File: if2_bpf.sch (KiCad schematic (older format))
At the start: 16 parts

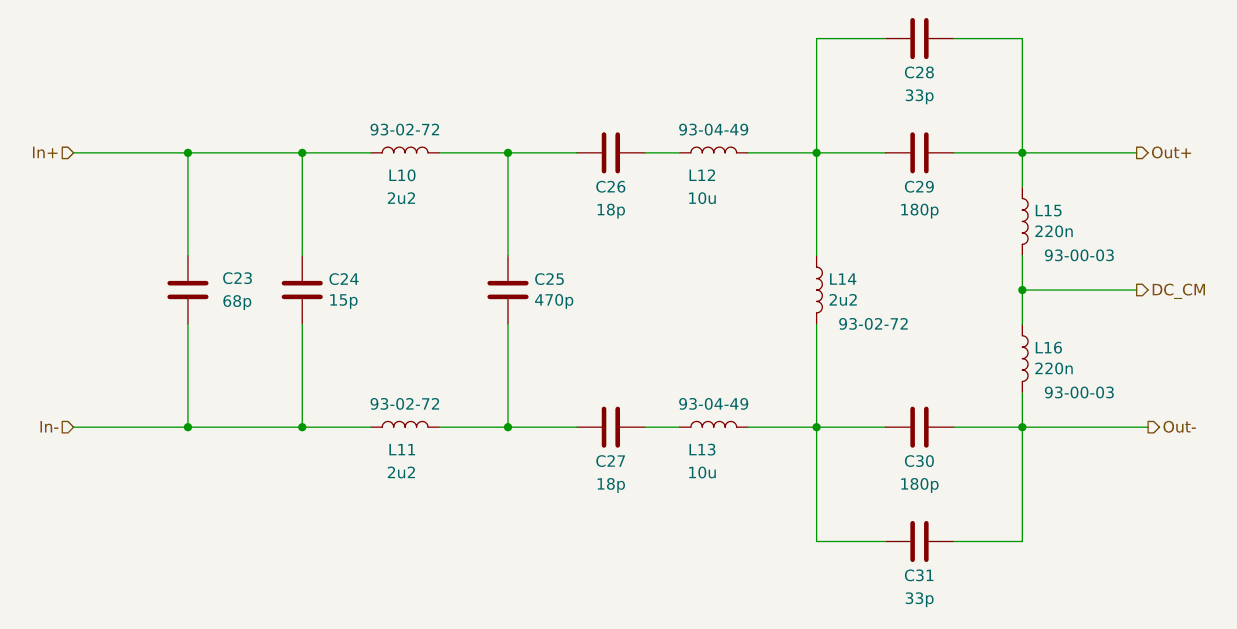
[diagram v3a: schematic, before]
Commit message: RX PCB revision: Diff amp + Mixer2
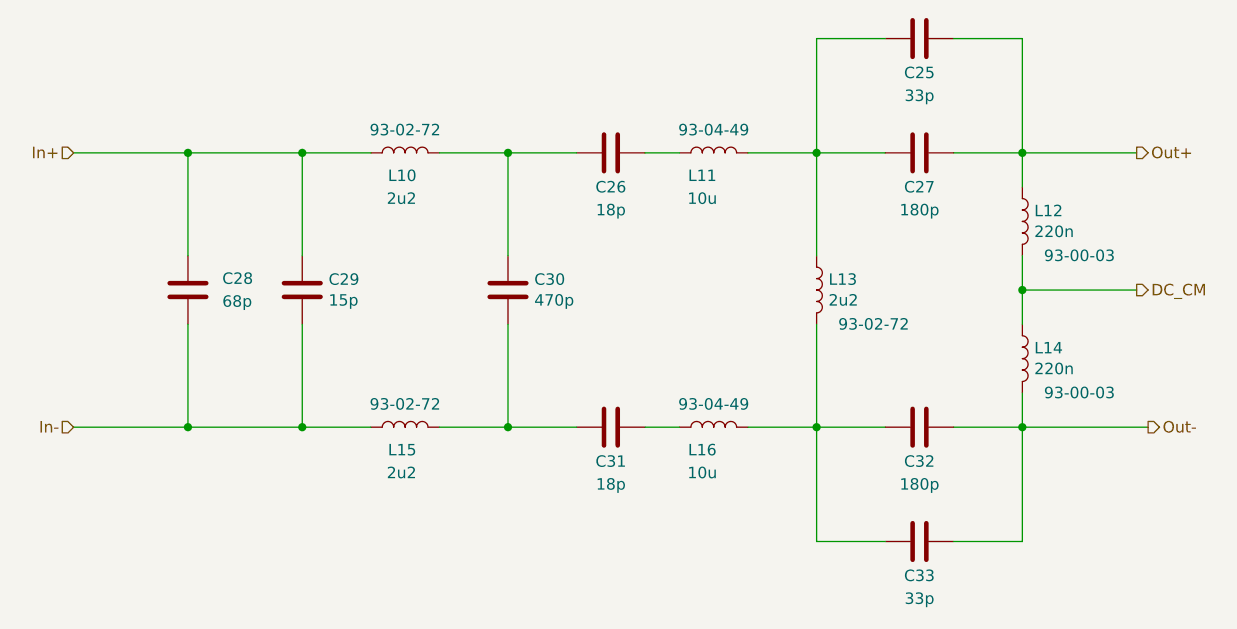
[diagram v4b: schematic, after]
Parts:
- C25: renamed from C28; footprint Capacitor_SMD:C_0805_2012Metric_Pad1.18x1.45mm_HandSolder -> Capacitor_SMD:C_0805_2012Metric_Pad1.15x1.40mm_HandSolder
- C26: footprint Capacitor_SMD:C_0805_2012Metric_Pad1.18x1.45mm_HandSolder -> Capacitor_SMD:C_0805_2012Metric_Pad1.15x1.40mm_HandSolder
- C27: renamed from C29; footprint Capacitor_SMD:C_0805_2012Metric_Pad1.18x1.45mm_HandSolder -> Capacitor_SMD:C_0805_2012Metric_Pad1.15x1.40mm_HandSolder
- C28: renamed from C23; footprint Capacitor_SMD:C_0805_2012Metric_Pad1.18x1.45mm_HandSolder -> Capacitor_SMD:C_0805_2012Metric_Pad1.15x1.40mm_HandSolder
- C29: renamed from C24; footprint Capacitor_SMD:C_0805_2012Metric_Pad1.18x1.45mm_HandSolder -> Capacitor_SMD:C_0805_2012Metric_Pad1.15x1.40mm_HandSolder
- C30: renamed from C25; footprint Capacitor_SMD:C_0805_2012Metric_Pad1.18x1.45mm_HandSolder -> Capacitor_SMD:C_0805_2012Metric_Pad1.15x1.40mm_HandSolder
- C31: renamed from C27; footprint Capacitor_SMD:C_0805_2012Metric_Pad1.18x1.45mm_HandSolder -> Capacitor_SMD:C_0805_2012Metric_Pad1.15x1.40mm_HandSolder
- C32: renamed from C30; footprint Capacitor_SMD:C_0805_2012Metric_Pad1.18x1.45mm_HandSolder -> Capacitor_SMD:C_0805_2012Metric_Pad1.15x1.40mm_HandSolder
- C33: renamed from C31; footprint Capacitor_SMD:C_0805_2012Metric_Pad1.18x1.45mm_HandSolder -> Capacitor_SMD:C_0805_2012Metric_Pad1.15x1.40mm_HandSolder
- renumbered L12 to L11, L15 to L12, L14 to L13, L16 to L14, L11 to L15, L13 to L16
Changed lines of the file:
@@
 $Descr A4 11693 8268
 encoding utf-8
-Sheet 6 7
+Sheet 5 7
 Title "9 MHz IF filter"
 Date "2021-01-15"
@@
 In-
 $Comp
-L Device:C C23
+L Device:C C28
 U 1 1 5FECCD6C
 P 4100 3950
-F 0 "C23" H 4250 4000 50  0000 L CNN
+F 0 "C28" H 4250 4000 50  0000 L CNN
 F 1 "68p" H 4250 3900 50  0000 L CNN
-F 2 "Capacitor_SMD:C_0805_2012Metric_Pad1.18x1.45mm_HandSolder" H 4138 3800 50  0001 C CNN
+F 2 "Capacitor_SMD:C_0805_2012Metric_Pad1.15x1.40mm_HandSolder" H 4138 3800 50  0001 C CNN
 F 3 "~" H 4100 3950 50  0001 C CNN
 	1    4100 3950
@@
 $EndComp
 $Comp
-L Device:C C24
+L Device:C C29
 U 1 1 5FECE707
 P 4600 3950
-F 0 "C24" H 4715 3996 50  0000 L CNN
+F 0 "C29" H 4715 3996 50  0000 L CNN
 F 1 "15p" H 4715 3905 50  0000 L CNN
-F 2 "Capacitor_SMD:C_0805_2012Metric_Pad1.18x1.45mm_HandSolder" H 4638 3800 50  0001 C CNN
+F 2 "Capacitor_SMD:C_0805_2012Metric_Pad1.15x1.40mm_HandSolder" H 4638 3800 50  0001 C CNN
 F 3 "~" H 4600 3950 50  0001 C CNN
 	1    4600 3950
@@
 F 0 "C26" V 6100 3350 50  0000 C CNN
 F 1 "18p" V 6200 3350 50  0000 C CNN
-F 2 "Capacitor_SMD:C_0805_2012Metric_Pad1.18x1.45mm_HandSolder" H 5988 3200 50  0001 C CNN
+F 2 "Capacitor_SMD:C_0805_2012Metric_Pad1.15x1.40mm_HandSolder" H 5988 3200 50  0001 C CNN
 F 3 "~" H 5950 3350 50  0001 C CNN
 	1    5950 3350
@@
 $EndComp
 $Comp
-L Device:L L12
+L Device:L L11
 U 1 1 5FECF5C4
 P 6400 3350
-F 0 "L12" V 6300 3400 50  0000 C CNN
+F 0 "L11" V 6300 3400 50  0000 C CNN
 F 1 "10u" V 6200 3400 50  0000 C CNN
 F 2 "Inductor_SMD:L_1210_3225Metric_Pad1.42x2.65mm_HandSolder" H 6400 3350 50  0001 C CNN
@@
 $EndComp
 $Comp
-L Device:L L14
+L Device:L L13
 U 1 1 5FED0166
 P 6850 3950
-F 0 "L14" H 6902 3996 50  0000 L CNN
+F 0 "L13" H 6902 3996 50  0000 L CNN
 F 1 "2u2" H 6902 3905 50  0000 L CNN
 F 2 "Inductor_SMD:L_0805_2012Metric_Pad1.15x1.40mm_HandSolder" H 6850 3950 50  0001 C CNN
@@
 $EndComp
 $Comp
-L Device:C C29
+L Device:C C27
 U 1 1 5FED1E6D
 P 7300 3350
-F 0 "C29" V 7450 3350 50  0000 C CNN
+F 0 "C27" V 7450 3350 50  0000 C CNN
 F 1 "180p" V 7550 3350 50  0000 C CNN
-F 2 "Capacitor_SMD:C_0805_2012Metric_Pad1.18x1.45mm_HandSolder" H 7338 3200 50  0001 C CNN
+F 2 "Capacitor_SMD:C_0805_2012Metric_Pad1.15x1.40mm_HandSolder" H 7338 3200 50  0001 C CNN
 F 3 "~" H 7300 3350 50  0001 C CNN
 	1    7300 3350
@@
 $EndComp
 $Comp
-L Device:L L15
+L Device:L L12
 U 1 1 5FED258A
 P 7750 3650
-F 0 "L15" H 7802 3696 50  0000 L CNN
+F 0 "L12" H 7802 3696 50  0000 L CNN
 F 1 "220n" H 7802 3605 50  0000 L CNN
 F 2 "Inductor_SMD:L_1210_3225Metric_Pad1.42x2.65mm_HandSolder" H 7750 3650 50  0001 C CNN
@@
 DC_CM
 $Comp
-L Device:C C30
+L Device:C C32
 U 1 1 5FED6CF7
 P 7300 4550
-F 0 "C30" V 7150 4550 50  0000 C CNN
+F 0 "C32" V 7150 4550 50  0000 C CNN
 F 1 "180p" V 7050 4550 50  0000 C CNN
-F 2 "Capacitor_SMD:C_0805_2012Metric_Pad1.18x1.45mm_HandSolder" H 7338 4400 50  0001 C CNN
+F 2 "Capacitor_SMD:C_0805_2012Metric_Pad1.15x1.40mm_HandSolder" H 7338 4400 50  0001 C CNN
 F 3 "~" H 7300 4550 50  0001 C CNN
 	1    7300 4550
@@
 $EndComp
 $Comp
-L Device:C C27
+L Device:C C31
 U 1 1 5FED7DBE
 P 5950 4550
-F 0 "C27" V 6100 4550 50  0000 C CNN
+F 0 "C31" V 6100 4550 50  0000 C CNN
 F 1 "18p" V 6200 4550 50  0000 C CNN
-F 2 "Capacitor_SMD:C_0805_2012Metric_Pad1.18x1.45mm_HandSolder" H 5988 4400 50  0001 C CNN
+F 2 "Capacitor_SMD:C_0805_2012Metric_Pad1.15x1.40mm_HandSolder" H 5988 4400 50  0001 C CNN
 F 3 "~" H 5950 4550 50  0001 C CNN
 	1    5950 4550
@@
 $EndComp
 $Comp
-L Device:C C25
+L Device:C C30
 U 1 1 5FEE51AD
 P 5500 3950
-F 0 "C25" H 5615 3996 50  0000 L CNN
+F 0 "C30" H 5615 3996 50  0000 L CNN
 F 1 "470p" H 5615 3905 50  0000 L CNN
-F 2 "Capacitor_SMD:C_0805_2012Metric_Pad1.18x1.45mm_HandSolder" H 5538 3800 50  0001 C CNN
+F 2 "Capacitor_SMD:C_0805_2012Metric_Pad1.15x1.40mm_HandSolder" H 5538 3800 50  0001 C CNN
 F 3 "~" H 5500 3950 50  0001 C CNN
 	1    5500 3950
@@
 $EndComp
 $Comp
-L Device:L L11
+L Device:L L15
 U 1 1 6002A199
 P 5050 4550
-F 0 "L11" V 4950 4500 50  0000 L CNN
+F 0 "L15" V 4950 4500 50  0000 L CNN
 F 1 "2u2" V 4850 4500 50  0000 L CNN
 F 2 "Inductor_SMD:L_0805_2012Metric_Pad1.15x1.40mm_HandSolder" H 5050 4550 50  0001 C CNN
@@
 $EndComp
 $Comp
-L Device:L L13
+L Device:L L16
 U 1 1 6002AC30
 P 6400 4550
-F 0 "L13" V 6300 4600 50  0000 C CNN
+F 0 "L16" V 6300 4600 50  0000 C CNN
 F 1 "10u" V 6200 4600 50  0000 C CNN
 F 2 "Inductor_SMD:L_1210_3225Metric_Pad1.42x2.65mm_HandSolder" H 6400 4550 50  0001 C CNN
@@
 $EndComp
 $Comp
-L Device:L L16
+L Device:L L14
 U 1 1 6002B609
 P 7750 4250
-F 0 "L16" H 7802 4296 50  0000 L CNN
+F 0 "L14" H 7802 4296 50  0000 L CNN
 F 1 "220n" H 7802 4205 50  0000 L CNN
 F 2 "Inductor_SMD:L_1210_3225Metric_Pad1.42x2.65mm_HandSolder" H 7750 4250 50  0001 C CNN
@@
 Connection ~ 7750 4550
 $Comp
-L Device:C C28
+L Device:C C25
 U 1 1 6002CCED
 P 7300 2850
-F 0 "C28" V 7450 2850 50  0000 C CNN
+F 0 "C25" V 7450 2850 50  0000 C CNN
 F 1 "33p" V 7550 2850 50  0000 C CNN
-F 2 "Capacitor_SMD:C_0805_2012Metric_Pad1.18x1.45mm_HandSolder" H 7338 2700 50  0001 C CNN
+F 2 "Capacitor_SMD:C_0805_2012Metric_Pad1.15x1.40mm_HandSolder" H 7338 2700 50  0001 C CNN
 F 3 "~" H 7300 2850 50  0001 C CNN
 	1    7300 2850
@@
 $EndComp
 $Comp
-L Device:C C31
+L Device:C C33
 U 1 1 6002D1C8
 P 7300 5050
-F 0 "C31" V 7150 5050 50  0000 C CNN
+F 0 "C33" V 7150 5050 50  0000 C CNN
 F 1 "33p" V 7050 5050 50  0000 C CNN
-F 2 "Capacitor_SMD:C_0805_2012Metric_Pad1.18x1.45mm_HandSolder" H 7338 4900 50  0001 C CNN
+F 2 "Capacitor_SMD:C_0805_2012Metric_Pad1.15x1.40mm_HandSolder" H 7338 4900 50  0001 C CNN
 F 3 "~" H 7300 5050 50  0001 C CNN
 	1    7300 5050
